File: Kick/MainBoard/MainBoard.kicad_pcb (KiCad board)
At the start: 4 copper layers, 128.8 x 67 mm, 41 parts, among them J1 CN1 / J11, J2 CN2 / J12, U0 NOIP1SN1300A-QTI, U1 NOIP1SN1300A-QTI, U2 NX3L4053, U3 NX3L4053, U4 MIC5504-1.8YM5

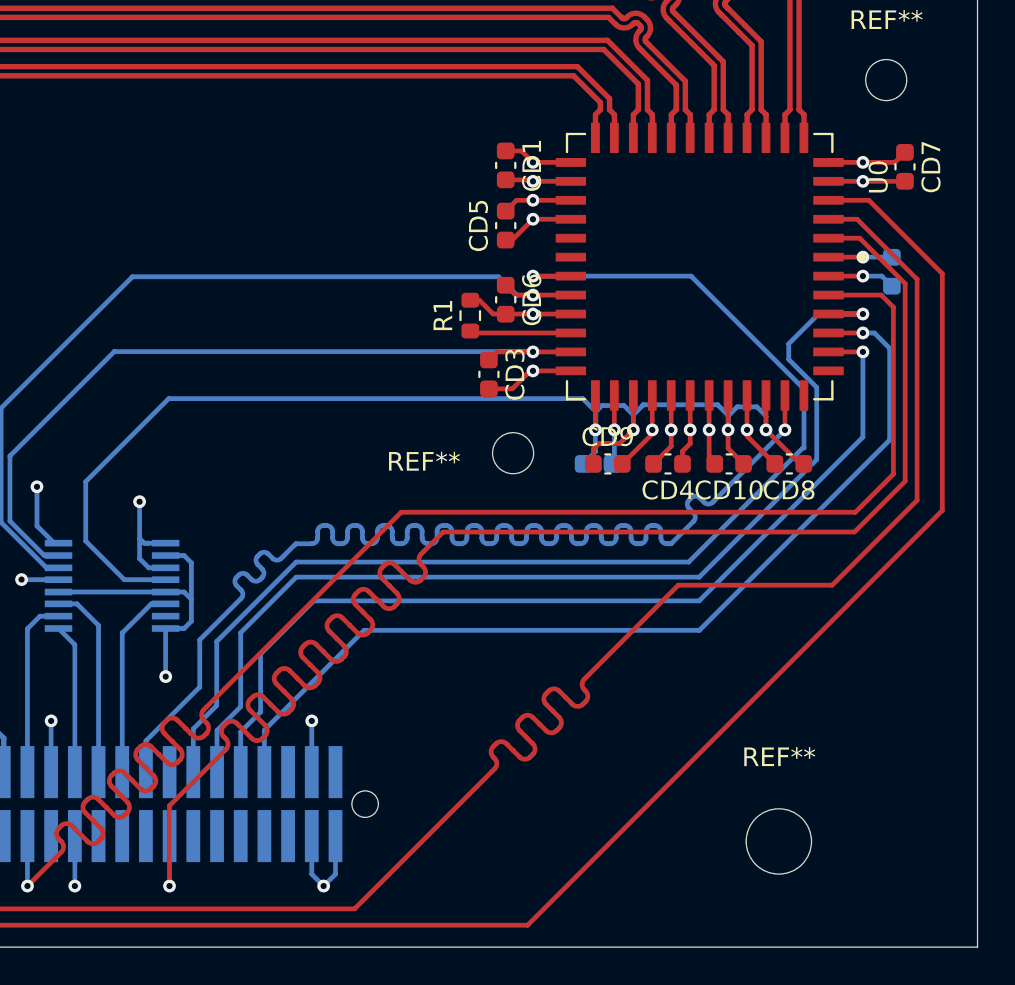
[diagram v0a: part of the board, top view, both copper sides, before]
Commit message: tried several connectors, chose TFML/SFML. routing LVDS witb 0 skew.
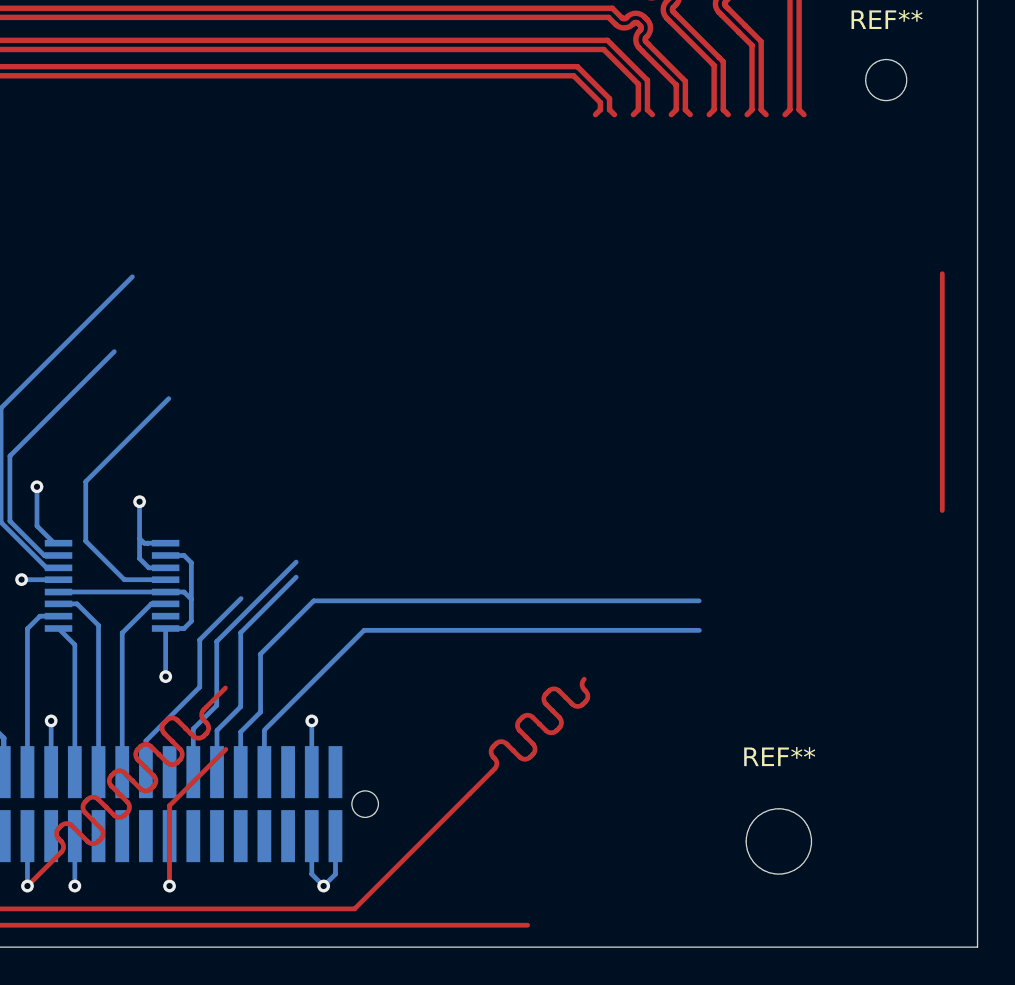
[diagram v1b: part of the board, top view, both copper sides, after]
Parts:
- removed CD1, CD10, CD11, CD2, CD3, CD4, CD5, CD6, CD7, CD8, CD9: 100nF, Capacitor_SMD:C_0603_1608Metric
- removed R1: 47k, Resistor_SMD:R_0603_1608Metric
- removed the REF** at (130.9, 83.4)
- removed U0: NOIP1SN1300A-QTI, NOIP1SN1300A-QTI:LCC101P1422X1422X228-48N
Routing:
- net /mosi: track 179.6 -> 99.9 mm
- net /vdd33_0: track 90.0 -> 14.8 mm, vias 4 -> 0
- net /vdd18_0: track 78.2 -> 20.2 mm, vias 3 -> 0
- net /trigger0_0: track 66.5 -> 11.4 mm, vias 1 -> 0
- net /vddpix_0: track 69.2 -> 14.6 mm, vias 4 -> 0
- net /ss_0: track 86.8 -> 33.5 mm
- net /noip_clk_0: track 65.5 -> 13.5 mm, vias 1 -> 0
- net GND: track 202.3 -> 156.7 mm, vias 50 -> 39
- net /resetn_0: track 56.0 -> 12.2 mm, vias 1 -> 0
- net /miso: track 162.1 -> 122.4 mm
- net /sck: track 172.9 -> 133.7 mm
- net /monitor1_0: track 50.7 -> 27.7 mm, vias 1 -> 0
- net /monitor0_0: track 50.3 -> 31.5 mm, vias 1 -> 0
- net Net-(U0-IBIAS_MASTER): track 5.46 -> 0.00 mm
- net /sync0_P: track 54.0 -> 52.8 mm
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
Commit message: routed PythonBreakout with SFML
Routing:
- net /sck: track 133.7 -> 121.0 mm

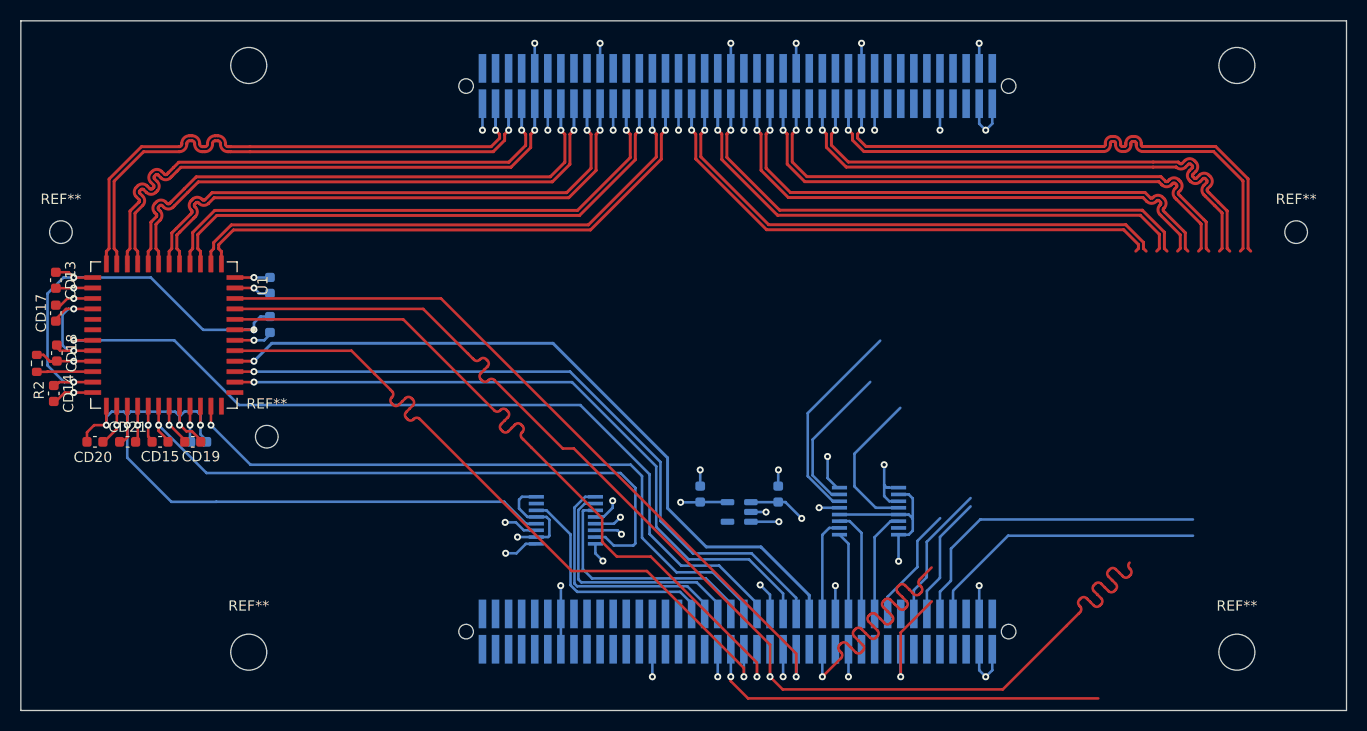
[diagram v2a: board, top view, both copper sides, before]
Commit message: routed 0 side on MainBoard with TFMLs
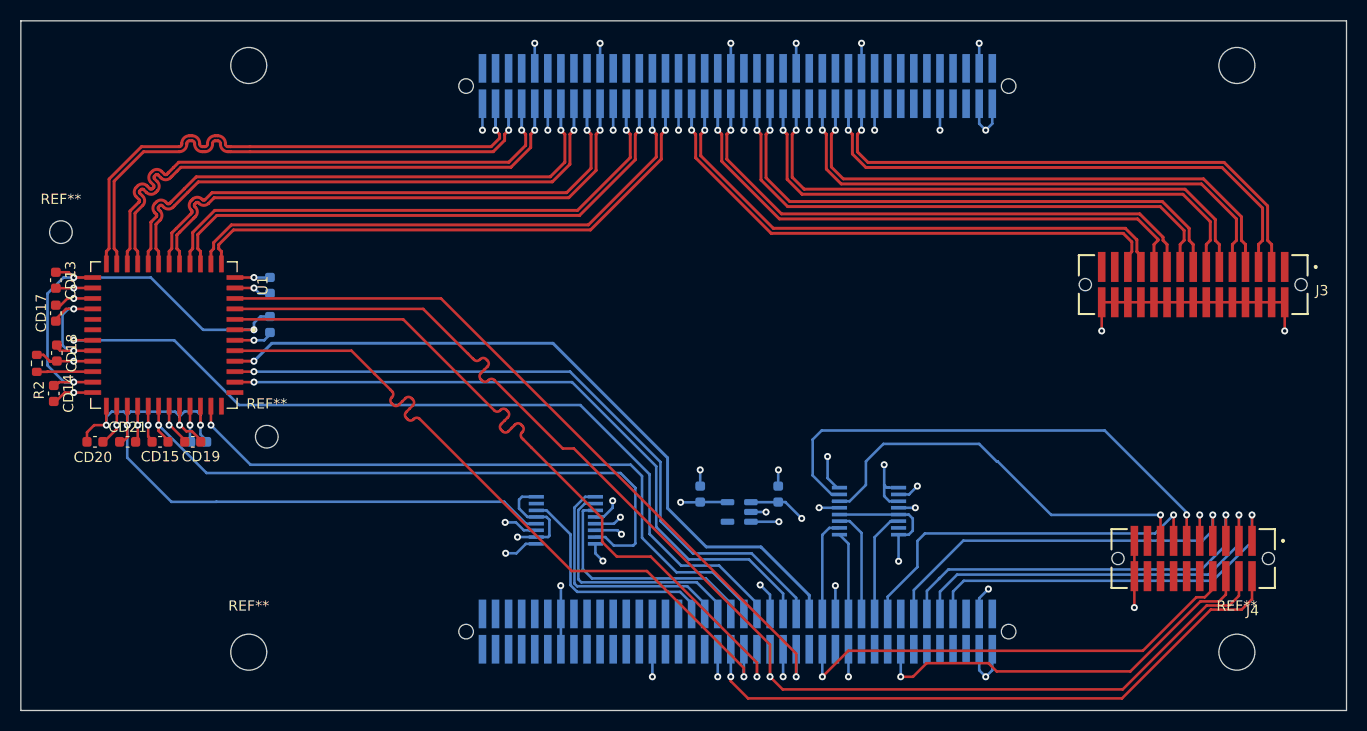
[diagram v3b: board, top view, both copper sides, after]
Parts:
- removed the REF** at (150.9, 63.4)
- added J3: Conn_02x15_Odd_Even, SAMTEC_TFML11502LDLC:SAMTEC_TFML-115-02-L-D-LC, F.Cu at (140.9, 68.5)
- added J4: Conn_02x10_Odd_Even, SAMTEC_TFML11002LDLC:SAMTEC_TFML-110-02-L-D-LC-TR, F.Cu at (140.9, 95.1)
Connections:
- J1 pad 13: /noip_clk_0 -> /trigger0_0
- J1 pad 17: /trigger0_0 -> /noip_clk_0
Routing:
- net /vdd33_0: track 14.8 -> 49.6 mm, vias 0 -> 1
- net /mosi: track 99.9 -> 128.7 mm
- net GND: track 156.7 -> 185.2 mm, vias 39 -> 43
- net /resetn_0: track 12.2 -> 38.7 mm, vias 0 -> 1
- net /trigger0_0: track 11.4 -> 37.8 mm, vias 0 -> 1
- net /noip_clk_0: track 13.5 -> 36.7 mm, vias 0 -> 1
- net /sck: track 121.0 -> 142.2 mm
- net /vdd18_0: track 20.2 -> 40.9 mm, vias 0 -> 1
- net /vddpix_0: track 14.6 -> 32.8 mm, vias 0 -> 2
- net /ss_0: track 33.5 -> 45.4 mm
- net /monitor1_0: track 27.7 -> 38.3 mm, vias 0 -> 1
- net /monitor0_0: track 31.5 -> 38.5 mm, vias 0 -> 1
- net /miso: track 122.4 -> 125.4 mm
- net /dout1_0_N: track 52.7 -> 54.9 mm
- net /dout1_0_P: track 52.7 -> 54.9 mm
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
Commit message: routed bottom part with length matching
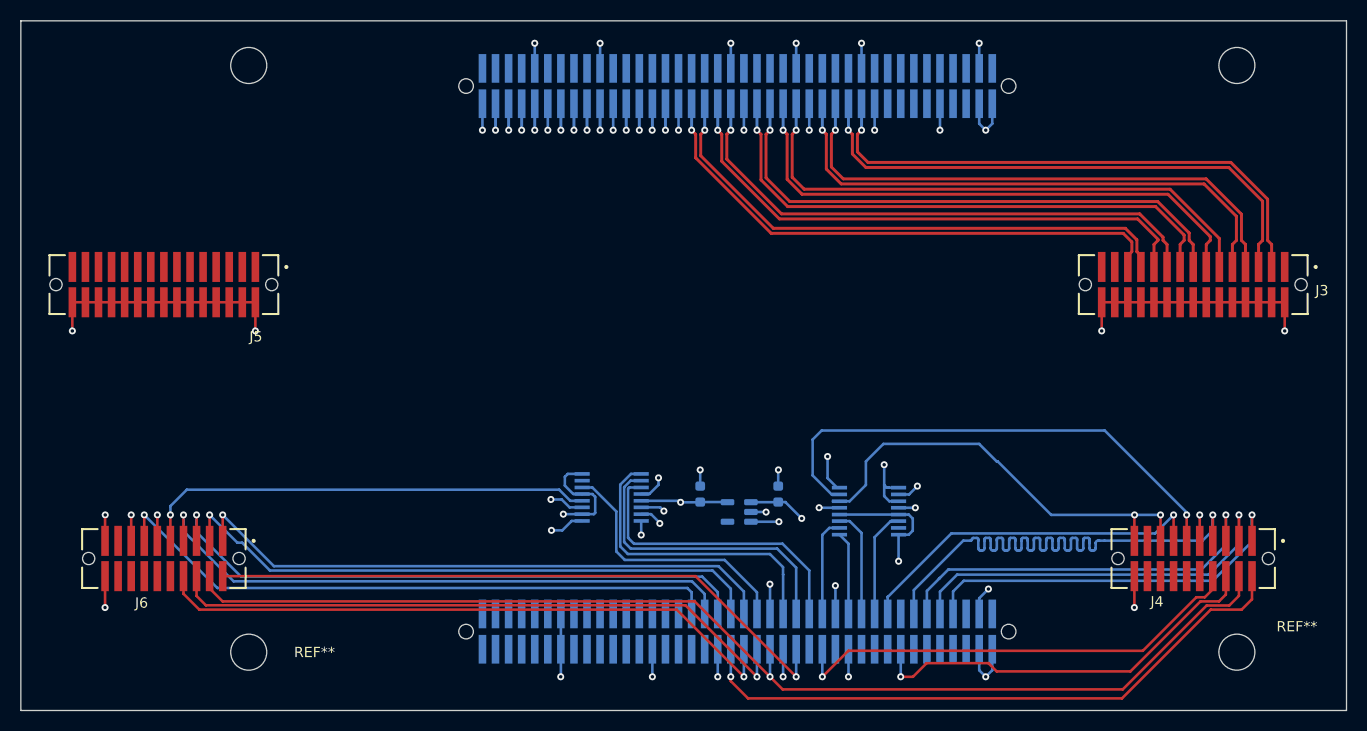
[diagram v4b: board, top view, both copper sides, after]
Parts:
- removed CD12, CD13, CD14, CD15, CD16, CD17, CD18, CD19, CD20, CD21, CD22: 100nF, Capacitor_SMD:C_0603_1608Metric
- removed R2: 47k, Resistor_SMD:R_0603_1608Metric
- removed the REF** at (30.9, 63.4)
- removed the REF** at (50.9, 83.3)
- removed U1: NOIP1SN1300A-QTI, NOIP1SN1300A-QTI:LCC101P1422X1422X228-48N
- added J5: Conn_02x15_Odd_Even, SAMTEC_TFML11502LDLC:SAMTEC_TFML-115-02-L-D-LC, F.Cu at (40.9, 68.5)
- added J6: Conn_02x10_Odd_Even, SAMTEC_TFML11002LDLC:SAMTEC_TFML-110-02-L-D-LC-TR, F.Cu at (40.9, 95.1)
- moved U3 4.98 mm to (84.4, 89.2)
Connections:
- J1 pad 29: /resetn_1 -> /vdd18_toggle_1
- J1 pad 31: /monitor1_1 -> /vdd33_toggle_1
- J1 pad 33: /monitor0_1 -> /vddpix_toggle_1
- J1 pad 37: /noip_clk_1 -> /sw_~{E}_1
- J1 pad 39: /trigger0_1 -> /monitor1_1
- J1 pad 41: /vdd18_toggle_1 -> /monitor0_1
- J1 pad 43: /vdd33_toggle_1 -> /resetn_1
- J1 pad 45: /vddpix_toggle_1 -> /trigger0_1
- J1 pad 47: /sw_~{E}_1 -> /noip_clk_1
- J4 pad 10: GND -> unconnected-(J4-Pin_10-Pad10)
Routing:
- net /vdd33_1: track 118.1 -> 55.5 mm, vias 4 -> 2
- net /dout0_1_P: track 54.1 -> 2.58 mm
- net /dout0_1_N: track 54.1 -> 2.58 mm
- net /clkout1_P: track 54.0 -> 2.58 mm
- net /clkout1_N: track 54.0 -> 2.58 mm
- net /dout2_1_P: track 53.9 -> 2.58 mm
- net /dout2_1_N: track 53.9 -> 2.58 mm
- net /dout1_1_N: track 53.9 -> 2.58 mm
- net /dout1_1_P: track 53.9 -> 2.58 mm
- net /dout3_1_P: track 53.9 -> 2.58 mm
- net /dout3_1_N: track 53.9 -> 2.58 mm
- net /sync1_P: track 53.8 -> 2.58 mm
- net /sync1_N: track 53.8 -> 2.58 mm
- net /vddpix_1: track 76.7 -> 44.5 mm, vias 4 -> 1
- net /vdd18_1: track 85.0 -> 60.4 mm, vias 4 -> 2
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
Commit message: routed all layers, length matched top part and updated models
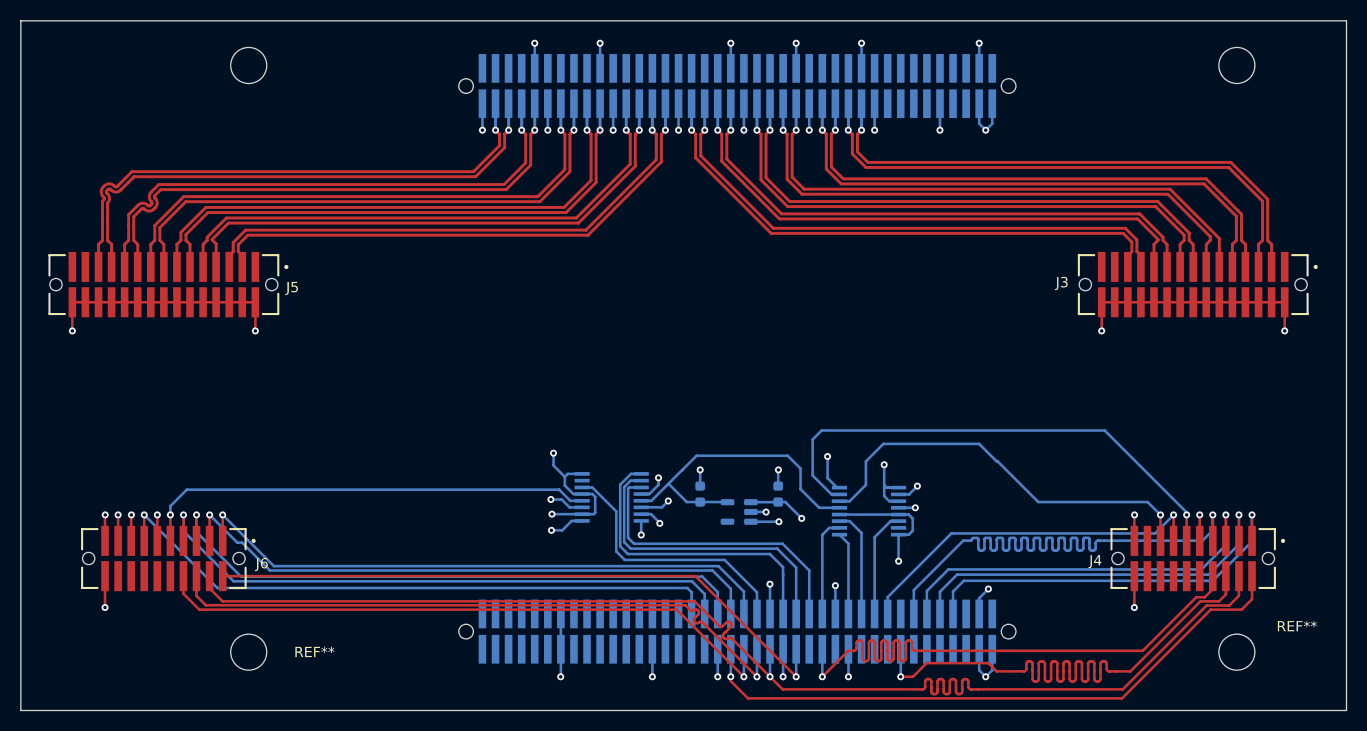
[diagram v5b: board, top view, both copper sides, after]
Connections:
- J6 pad 15: /vdd18_1 -> GND
- J6 pad 17: unconnected-(J6-Pin_17-Pad17) -> /vdd18_1
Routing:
- net /dout0_1_N: track 2.58 -> 53.1 mm
- net /dout0_1_P: track 2.58 -> 53.1 mm
- net /dout1_1_P: track 2.58 -> 53.1 mm
- net /dout1_1_N: track 2.58 -> 53.1 mm
- net /dout2_1_P: track 2.58 -> 52.8 mm
- net /dout2_1_N: track 2.58 -> 52.8 mm
- net /dout3_1_P: track 2.58 -> 52.8 mm
- net /dout3_1_N: track 2.58 -> 52.8 mm
- net /sync1_N: track 2.58 -> 52.7 mm
- net /sync1_P: track 2.58 -> 52.7 mm
- net /clkout1_P: track 2.58 -> 52.6 mm
- net /clkout1_N: track 2.58 -> 52.6 mm
- net /mosi: track 117.4 -> 141.1 mm
- net /ss_0: track 45.4 -> 61.1 mm
- net /miso: track 113.6 -> 124.9 mm
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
